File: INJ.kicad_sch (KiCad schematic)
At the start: 10 parts, among them U2 VNLD5160TR-E, U3 VNLD5160TR-E

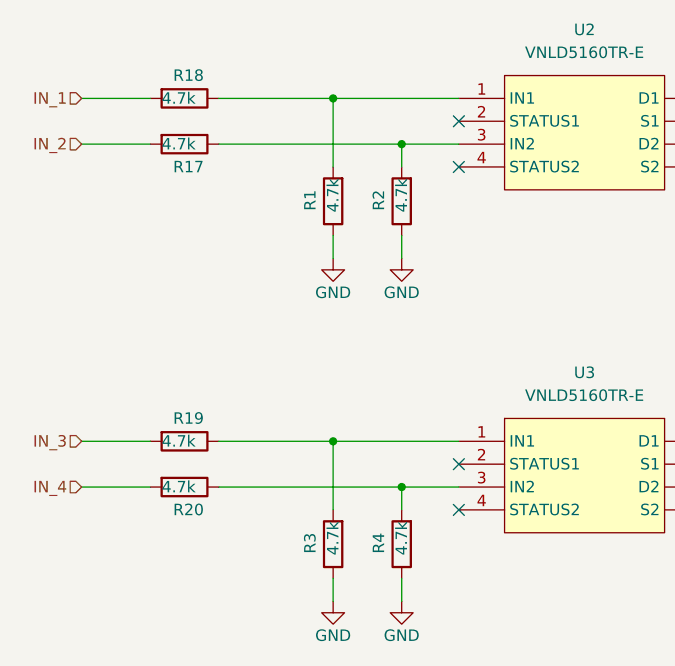
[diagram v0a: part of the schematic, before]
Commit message: Stupid mistake — I ended up making a voltage divider instead of a protection circuit. I'm the best.
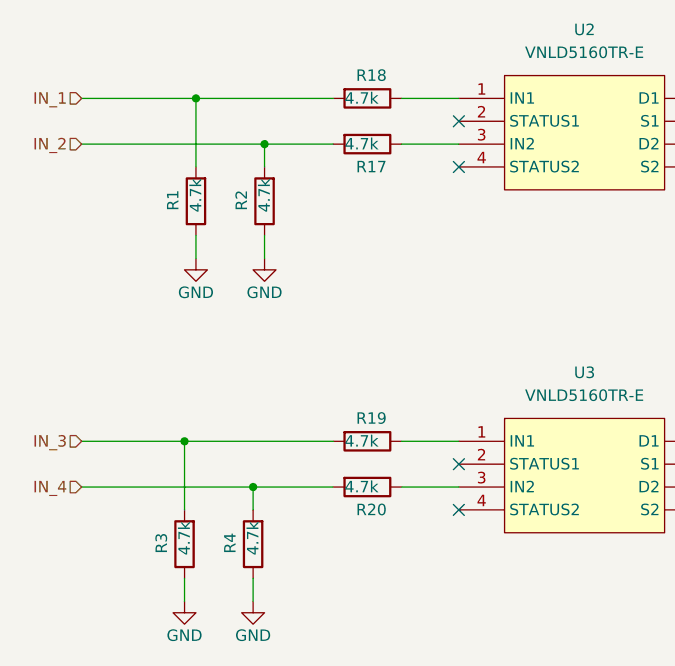
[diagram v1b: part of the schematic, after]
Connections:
- net IN_1: now also R1.2
- net IN_2: now also R2.2
- net IN_3: now also R3.2
- net IN_4: now also R4.2
- net at R18.1, U2.1 (IN1): no longer R1.2
- net at R19.1, U3.1 (IN1): no longer R3.2
- net at R20.1, U3.3 (IN2): no longer R4.2
- net at R17.1, U2.3 (IN2): no longer R2.2
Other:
- moved on the sheet: R1, R17, R18, R19, R2, R20, R3, R4

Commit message: Rev D
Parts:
- removed R17, R18, R19, R20: 4.7k, Hellen:R0603, symbol Device:R
- removed U2, U3: VNLD5160TR-E, Package_SO:SOIC-8_3.9x4.9mm_P1.27mm, symbol chips:VNLD5160
- added C29, C30: 100n, Capacitor_SMD:C_0603_1608Metric, symbol Device:C
- added Q1, Q2, Q3, Q4: VND14NV04TR-E, Package_TO_SOT_SMD:TO-252-2, symbol semiconductors:VND14NV04TR-E
- added U2: SN74LVC4245APWR, EasyEda2Kicad:TSSOP-24_L7.8-W4.4-P0.65-LS6.4-BL, symbol easyeda2kicad:SN74LVC4245APWR
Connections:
- net GND: now also C29.1, C30.1, Q1.3 (S), Q2.3 (S), Q3.3 (S), Q4.3 (S), U2.11 (GND), U2.12 (GND), U2.13 (GND), U2.2 (DIR), U2.22 (~{OE})
- net IN_1: now also U2.18 (B4); no longer R1.2
- net IN_2: now also U2.19 (B3); no longer R2.2
- net IN_3: now also U2.20 (B2); no longer R3.2
- net IN_4: now also U2.21 (B1); no longer R4.2
- net OUT_1: now also Q1.2 (D)
- net OUT_2: now also Q2.2 (D)
- net OUT_3: now also Q3.2 (D)
- net OUT_4: now also Q4.2 (D)
- new net +3.3VA: C30.2, U2.23 (VCCB), U2.24 (VCCB)
- new net +5VA: C29.2, U2.1 (VCCA)
- new net OUT_5V_1: Q1.1 (G), R1.2, U2.6 (A4)
- new net OUT_5V_2: Q2.1 (G), R2.2, U2.5 (A3)
- new net OUT_5V_3: Q3.1 (G), R3.2, U2.4 (A2)
- new net OUT_5V_4: Q4.1 (G), R4.2, U2.3 (A1)
- no-connect marks 4 -> 8

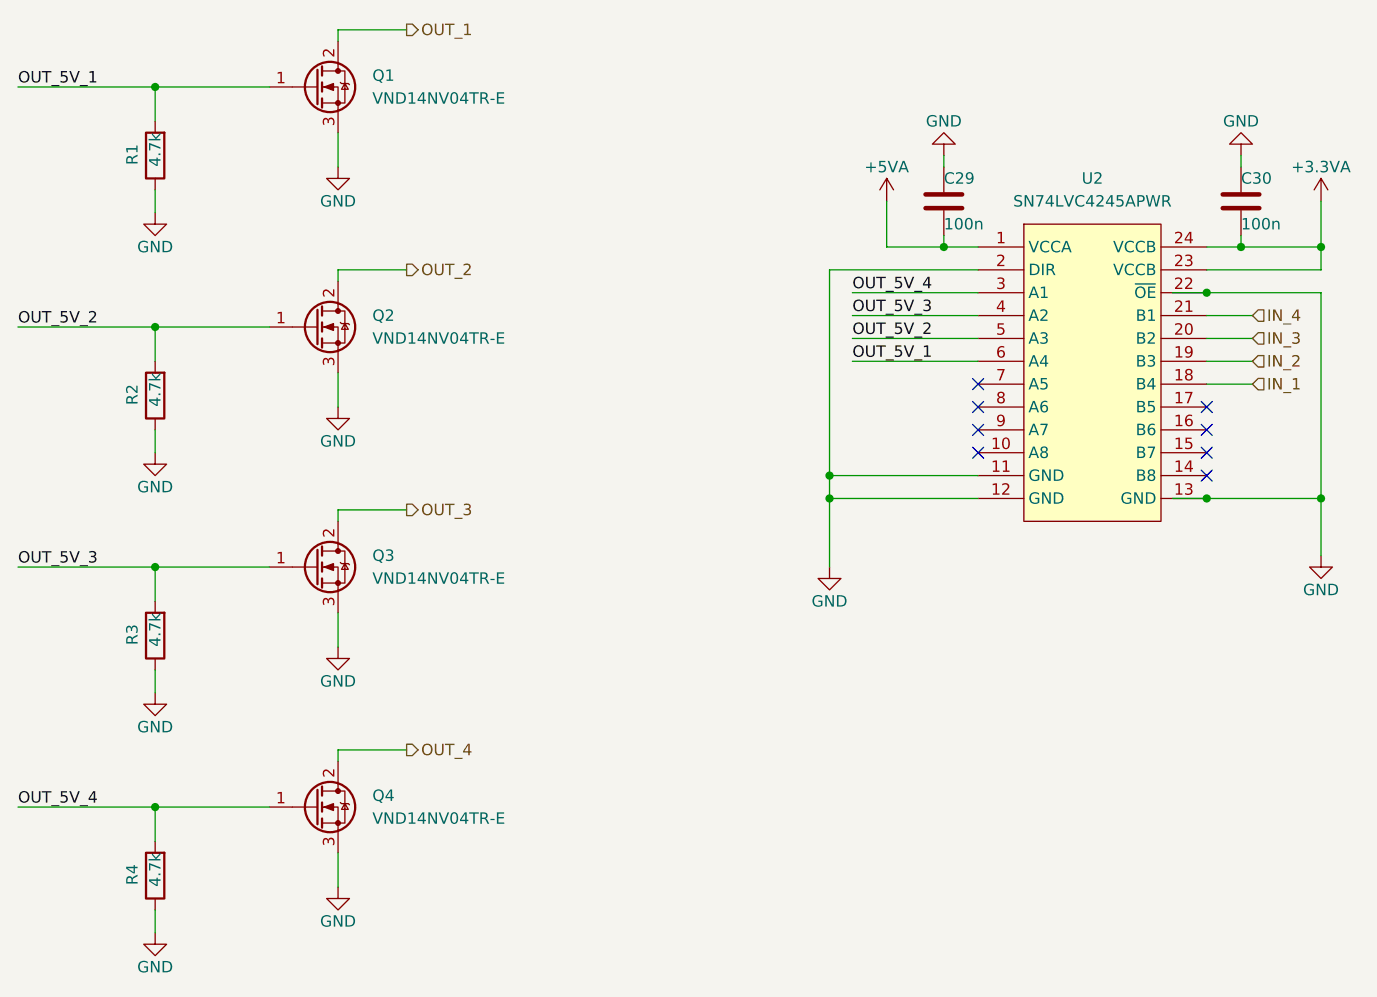
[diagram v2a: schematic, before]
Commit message: Rev E
Back to VNLD5160TR-E, 1 channel per injector now
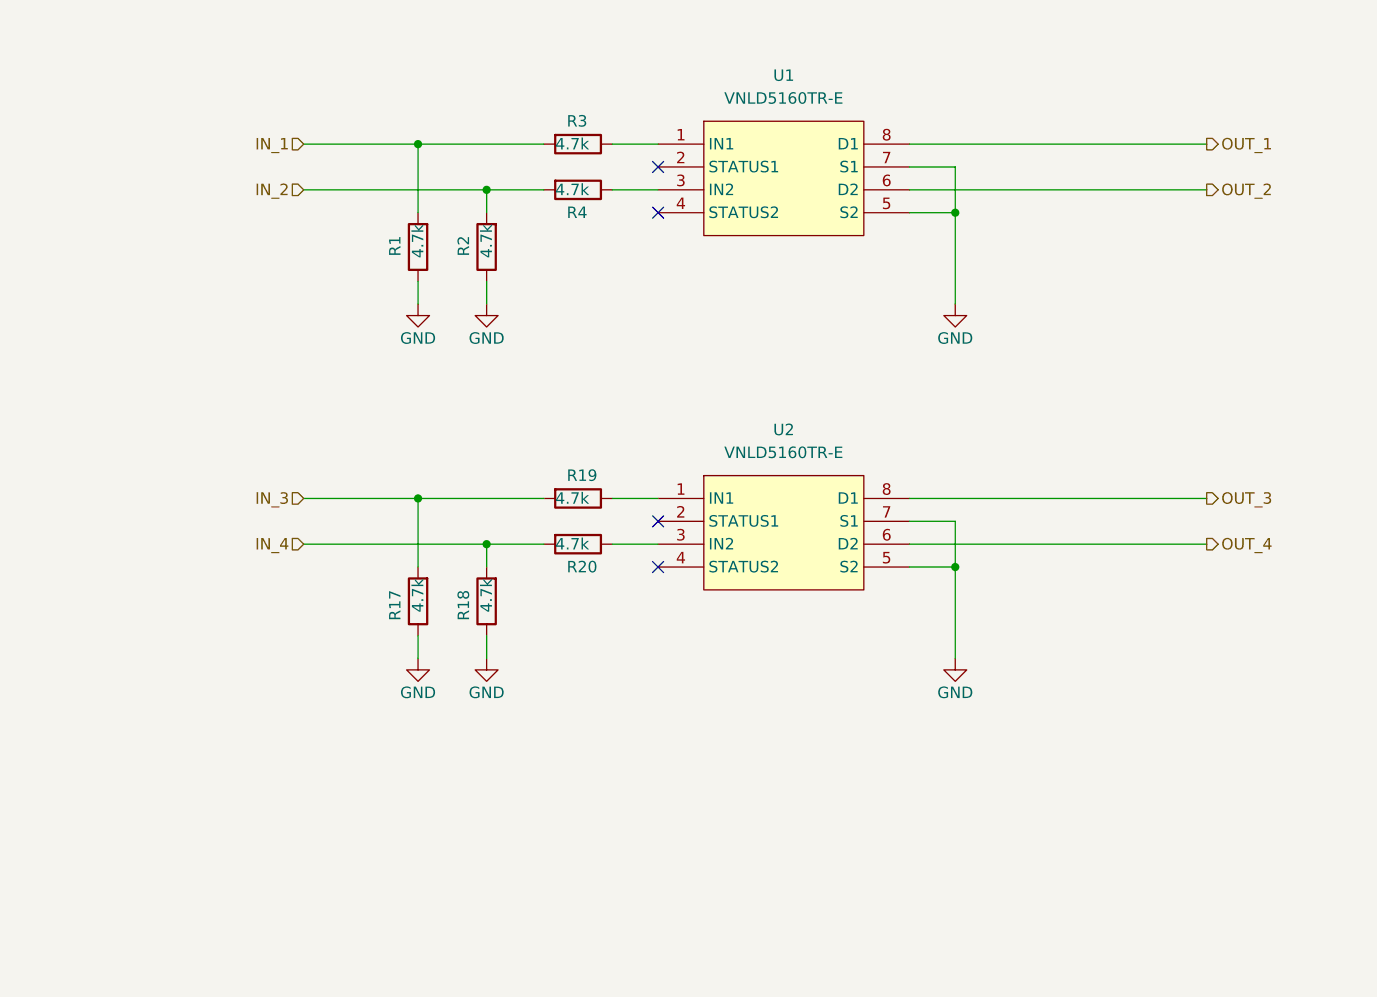
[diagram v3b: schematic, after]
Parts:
- removed C29, C30: 100n, Capacitor_SMD:C_0603_1608Metric, symbol Device:C
- removed Q1, Q2, Q3, Q4: VND14NV04TR-E, Package_TO_SOT_SMD:TO-252-2, symbol semiconductors:VND14NV04TR-E
- removed U2: SN74LVC4245APWR, EasyEda2Kicad:TSSOP-24_L7.8-W4.4-P0.65-LS6.4-BL, symbol easyeda2kicad:SN74LVC4245APWR
- added R17, R18, R19, R20: 4.7k, Hellen:R0603, symbol Device:R
- added U1, U2: VNLD5160TR-E, Package_SO:SOIC-8_3.9x4.9mm_P1.27mm, symbol chips:VNLD5160
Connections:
- net OUT_5V_1 is gone; now on net IN_1: R1.2
- net OUT_5V_2 is gone; now on net IN_2: R2.2
- net OUT_5V_3 is gone; now on net IN_1: R3.2
- net OUT_5V_4 is gone; now on net IN_2: R4.2
- net GND: now also R17.1, R18.1, U1.5 (S2), U1.7 (S1), U2.5 (S2), U2.7 (S1); no longer R3.1, R4.1
- net IN_3: now also R17.2, R19.2
- net IN_4: now also R18.2, R20.2
- net OUT_1: now also U1.8 (D1)
- net OUT_2: now also U1.6 (D2)
- net OUT_3: now also U2.8 (D1)
- net OUT_4: now also U2.6 (D2)
- new net: R3.1, U1.1 (IN1)
- new net: R4.1, U1.3 (IN2)
- new net: R19.1, U2.1 (IN1)
- new net: R20.1, U2.3 (IN2)
- no-connect marks 8 -> 4
